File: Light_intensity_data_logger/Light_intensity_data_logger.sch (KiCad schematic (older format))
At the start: 23 parts, among them J1 Wire_to_Vbat, Q1 Q_NMOS_GSD, U1 BME280, U2 TCS34725FN, U3 TSL25911FN, U4 Teensy3.6, U5 TS12A4514DBVR

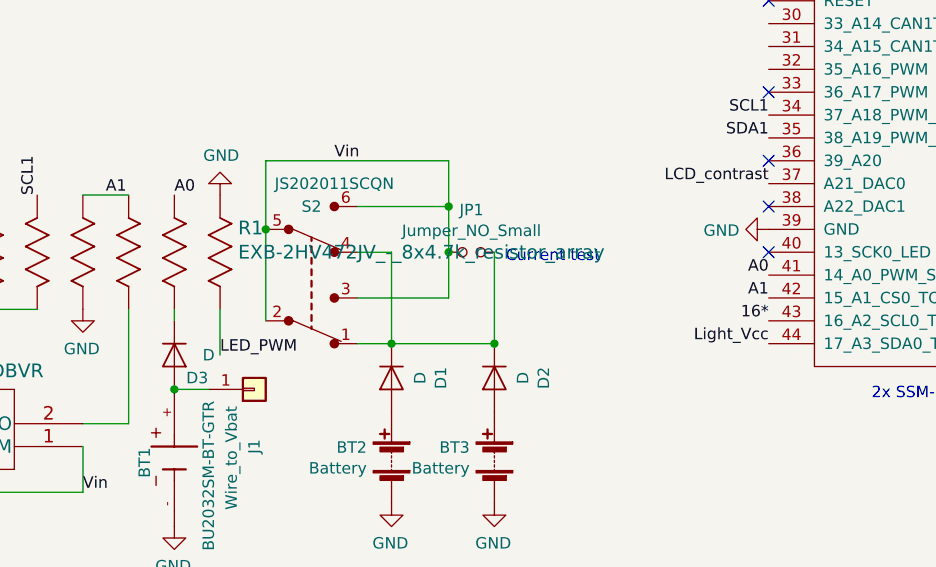
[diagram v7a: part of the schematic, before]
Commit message: Remove Vbat check circuit
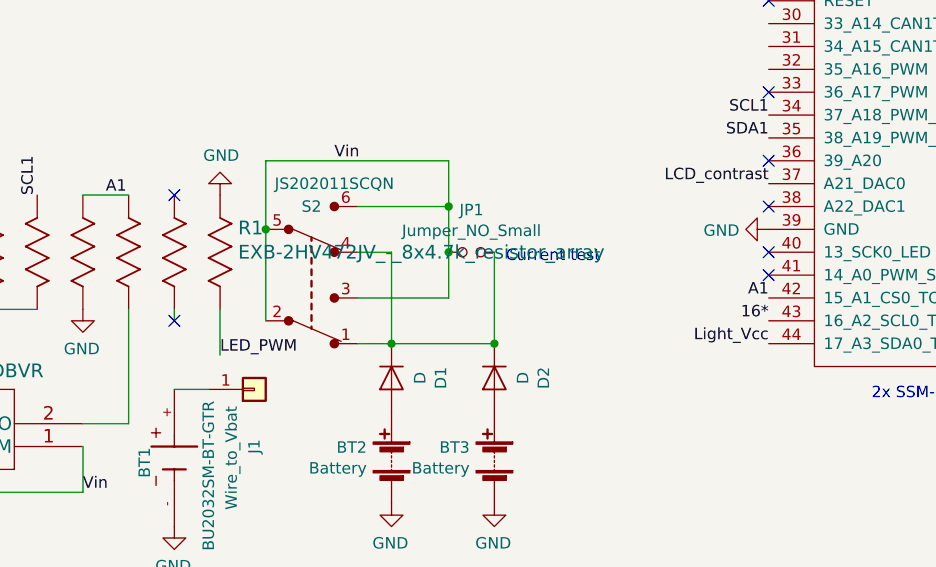
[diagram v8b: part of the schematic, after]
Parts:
- removed D3: D, Diodes_SMD:D_SOD-323, symbol device:D
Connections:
- net A0: no longer names the net of R1.2
- net A0: no longer U4.41 (14_A0_PWM_SCK0)
- no-connect marks 53 -> 56
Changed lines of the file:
@@
 Text Label 8300 3300 2    50   ~ 0
 Wire_to_coin_cell
-Text Label 5700 4550 0    50   ~ 0
-A0
 Text Label 5400 4550 0    50   ~ 0
 A1
@@
 	0    -1   1    0
 $EndComp
-$Comp
-L device:D D3
-U 1 1 5E2E8394
-P 5700 5250
-F 0 "D3" V 5800 5350 50  0000 C CNN
-F 1 "D" V 5700 5400 50  0000 C CNN
-F 2 "Diodes_SMD:D_SOD-323" H 5700 5250 50  0001 C CNN
-F 3 "https://toshiba.semicon-storage.com/info/docget.jsp?did=14077&prodName=CUS10S30" H 5700 5250 50  0001 C CNN
-F 4 "CUS10S30H3FCT-ND" H 5700 5250 50  0001 C CNN "Part#"
-	1    5700 5250
-	0    1    1    0
-$EndComp
 Text Label 3950 3150 2    50   ~ 0
 SDA0
@@
 Wire Wire Line
 	2350 1000 2050 1000
-Text Label 8300 4900 2    50   ~ 0
-A0
 $Comp
 L device:C C2
@@
 Text Label 2450 2300 0    50   ~ 0
 LED_PWM
-Connection ~ 5700 5400
 Text Label 8300 5000 2    50   ~ 0
 A1
@@
 	1    0    0    1
 $EndComp
+NoConn ~ 8300 4900
+NoConn ~ 5700 5100
+NoConn ~ 5700 4550
 $EndSCHEMATC
